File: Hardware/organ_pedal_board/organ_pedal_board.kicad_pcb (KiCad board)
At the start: 2 copper layers, 100 x 100 mm, 42 parts, among them J1 Conn_01x04, J2 NMJ6HFD2, J3 NMJ6HFD2, J4 ADS1115_conn, SW1 SW_Push, SW2 SW_Push, SW3 SW_Push, SW4 SW_Push, SW5 SW_Push, SW6 SW_Push, SW7 SW_Push, SW8 SW_Push, SW9 SW_Push, U1 MCP6002-xSN

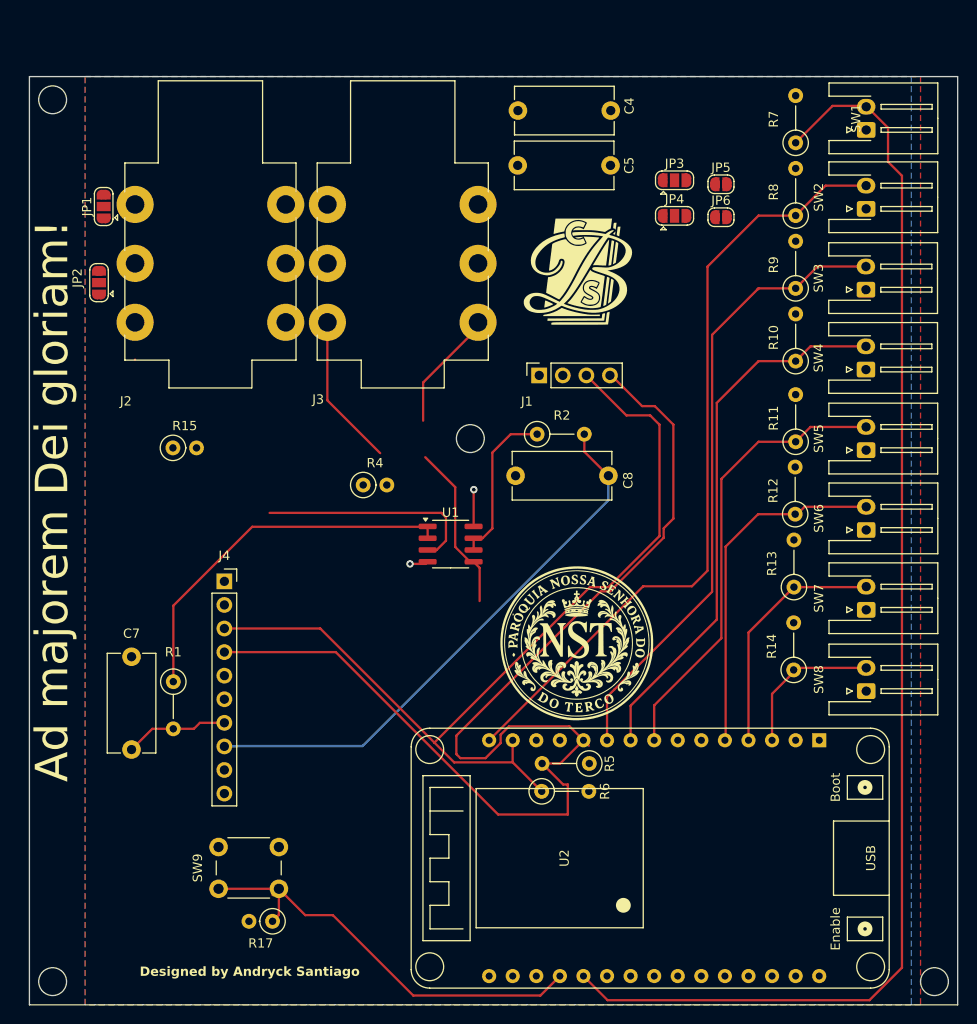
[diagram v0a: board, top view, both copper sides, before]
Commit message: Update organ pedal hardware design
Co-authored-by: Copilot <223556219+Copilot@users.noreply.github.com>
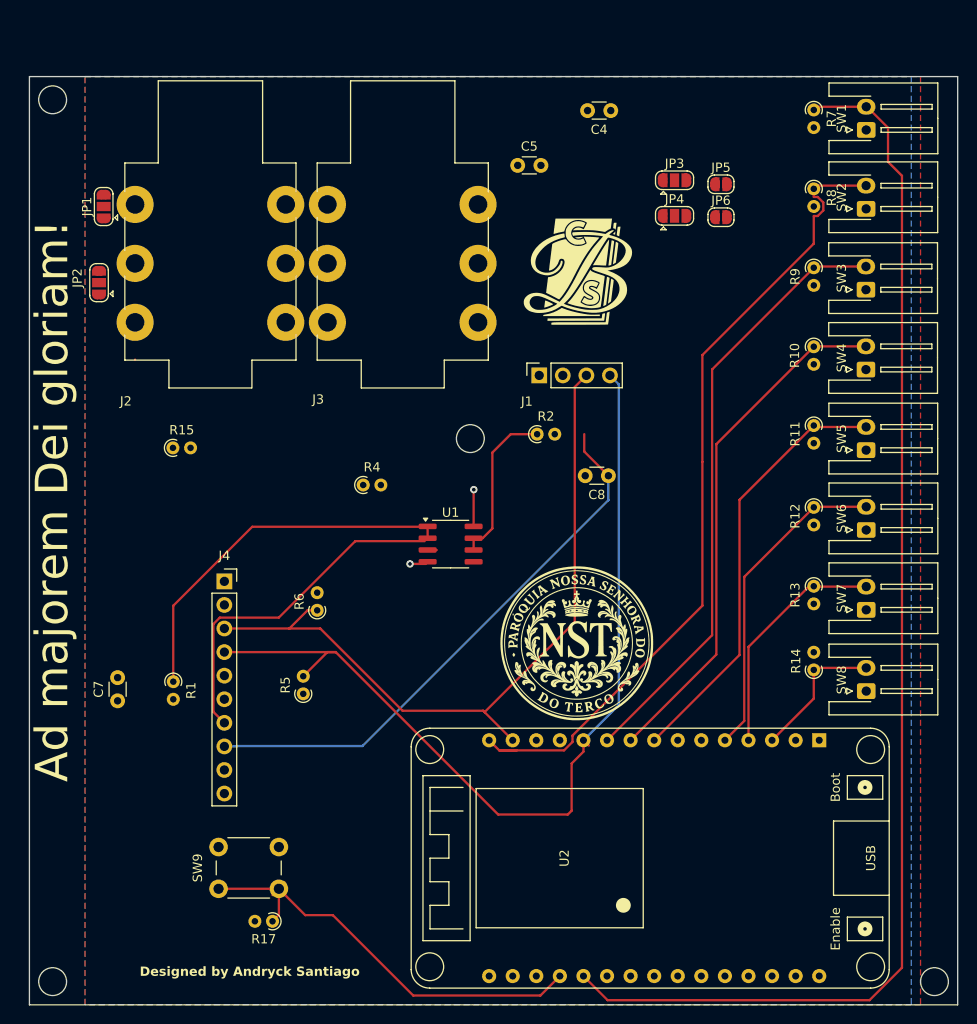
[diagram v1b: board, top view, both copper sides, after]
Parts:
- C4, C5, C7, C8: footprint Capacitor_THT:C_Disc_D10.5mm_W5.0mm_P10.00mm -> Capacitor_THT:C_Disc_D3.0mm_W1.6mm_P2.50mm
- R1, R10, R11, R12, R13, R14, R2, R5, R6, R7, R8, R9: footprint Resistor_THT:R_Axial_DIN0207_L6.3mm_D2.5mm_P5.08mm_Vertical -> Resistor_THT:R_Axial_DIN0204_L3.6mm_D1.6mm_P1.90mm_Vertical
- R15, R17, R4: footprint Resistor_THT:R_Axial_DIN0207_L6.3mm_D2.5mm_P2.54mm_Vertical -> Resistor_THT:R_Axial_DIN0204_L3.6mm_D1.6mm_P1.90mm_Vertical
- moved R5 31.7 mm to (144.5, 116.5), turned to 90 degrees
- moved R6 31.1 mm to (146.0, 107.5), turned to 90 degrees
- moved C7 5.46 mm to (124.5, 117.2)
- moved R7 4.04 mm to (199.5, 53.6), turned to -90 degrees
- moved R8 3.48 mm to (199.5, 62.1), turned to -90 degrees
- moved R9 2.96 mm to (199.5, 70.6), turned to -90 degrees
- moved R11 2.62 mm to (199.5, 87.6), turned to -90 degrees
- moved R10 2.50 mm to (199.5, 79.1), turned to -90 degrees
- moved R14 2.17 mm to (199.5, 113.9)
- moved R13 2.14 mm to (199.5, 104.9), turned to -90 degrees
- moved R12 2.14 mm to (199.5, 96.4), turned to -90 degrees
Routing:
- net /i2c_sda: track 129.1 -> 100.1 mm
- net /pedal1_signal: track 11.2 -> 37.6 mm
- net Net-(U1A-+): track 24.1 -> 0.97 mm
- net /i2c_scl: track 99.4 -> 80.7 mm
- net Net-(U1B-+): track 18.2 -> 0.38 mm
- net Net-(JP3-A): track 15.9 -> 0.00 mm
- net unconnected-(J3-PadTN): track 13.0 -> 0.57 mm
- net /button2: track 84.6 -> 89.2 mm
- net /button1: track 140.5 -> 137.1 mm
- net /button6: track 38.1 -> 34.7 mm
- net /button4: track 59.4 -> 56.8 mm
- net /button3: track 68.7 -> 66.3 mm
- net /button5: track 49.1 -> 46.7 mm
- net /button8: track 16.7 -> 15.2 mm
- net /button7: track 26.3 -> 25.5 mm

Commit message: Update organ pedal hardware design
Co-authored-by: Copilot <223556219+Copilot@users.noreply.github.com>
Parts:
- added REF**: logo_aslabz, organ_pedal_board:logo_aslabz, F.Cu at (126.5, 140.5)
- added REF**: logo_aslabz, organ_pedal_board:logo_aslabz, F.Cu at (177.0, 97.5)
- moved C4 85.6 mm to (124.5, 120.8), turned to -90 degrees
- moved C5 80.9 mm to (124.4, 128.0), turned to 90 degrees
- moved JP5 60.5 mm to (134.5, 86.7), turned to 180 degrees
- moved G*** 53.4 mm to (186.0, 59.0)
- moved R6 48.9 mm to (187.0, 134.1), turned to -90 degrees
- moved R5 42.7 mm to (182.5, 135.9)
- moved JP4 42.1 mm to (148.5, 86.7), turned to -90 degrees
- moved JP6 40.7 mm to (155.0, 86.7), turned to 180 degrees
- moved C7 38.6 mm to (161.8, 107.0), turned to 180 degrees
- moved JP3 34.4 mm to (161.5, 86.7), turned to -90 degrees
- moved R1 24.9 mm to (133.6, 90.5), turned to 0 degrees
- moved R15 24.1 mm to (154.1, 94.5)
- moved C8 23.8 mm to (161.8, 111.0)
- moved JP1 23.4 mm to (128.5, 86.7), turned to -90 degrees
- moved JP2 23.1 mm to (140.5, 86.7), turned to -90 degrees
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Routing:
- net (no net): track 57.9 -> 0.00 mm
- net Net-(JP3-B): track 0.00 -> 41.8 mm
- net Net-(U1A-+): track 0.97 -> 42.1 mm, vias 0 -> 1
- net Net-(JP1-B): track 0.00 -> 34.5 mm
- net +3.3V: track 3.97 -> 38.1 mm, vias 1 -> 2
- net Net-(U1B-+): track 0.38 -> 33.1 mm, vias 0 -> 1
- net /i2c_scl: track 80.7 -> 106.1 mm
- net Net-(JP3-A): track 0.00 -> 22.4 mm
- net /pedal2_signal: track 60.5 -> 38.3 mm, vias 0 -> 1
- net Net-(JP1-A): track 0.02 -> 21.8 mm
- net /pedal2_raw: track 0.00 -> 11.8 mm, vias 0 -> 1
- net Net-(JP5-B): track 0.00 -> 11.4 mm, vias 0 -> 1
- net Net-(JP6-B): track 0.00 -> 11.3 mm, vias 0 -> 1
- net /pedal1_raw: track 0.00 -> 10.8 mm, vias 0 -> 1
- net /pedal1_signal: track 37.6 -> 40.1 mm
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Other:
- outline, holes or cut-outs redrawn
